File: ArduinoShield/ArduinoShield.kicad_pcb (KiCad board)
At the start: 2 copper layers, 47 x 45.7 mm, 45 parts, among them J1 Molex 1053131103, J2 Molex 1053131102, J3 Molex 1053131103, J4 Molex 1053131102, J5 Molex 1053131102, U1 MCP9808_DFN, U2 ALS31300, U3 BME280

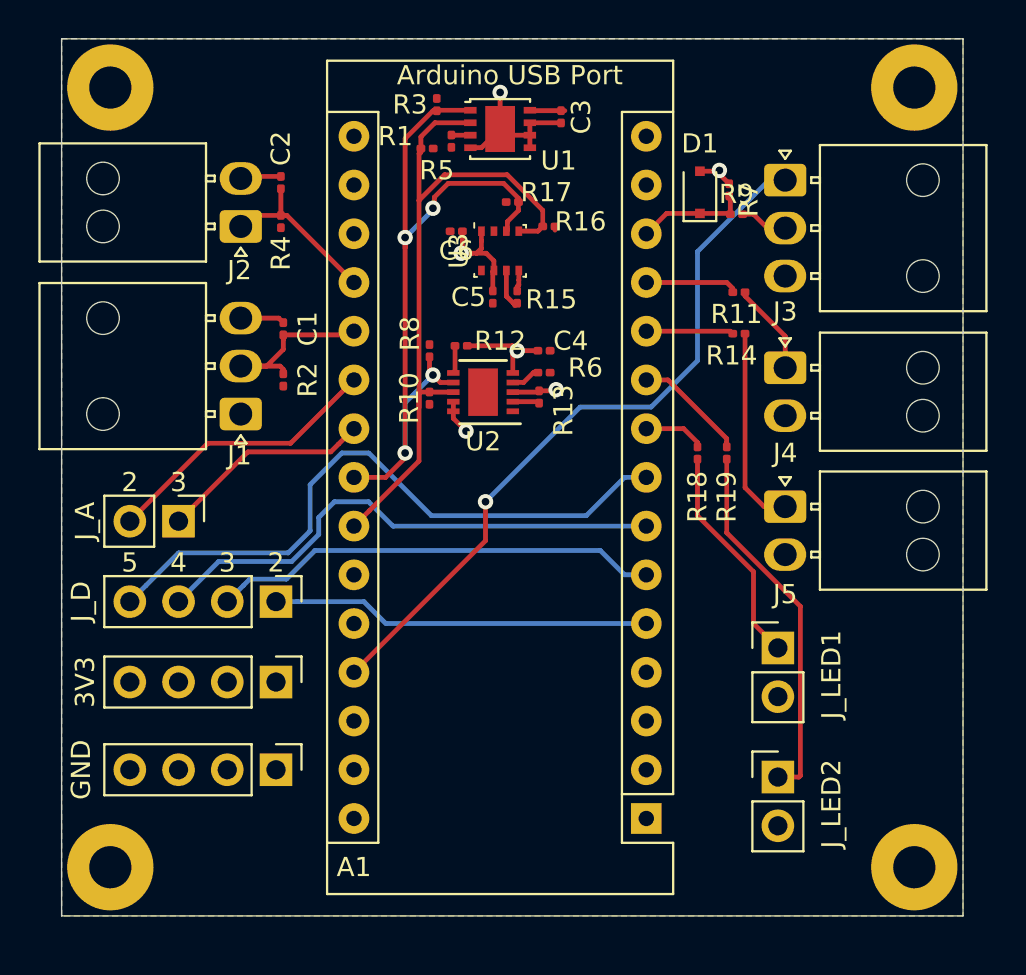
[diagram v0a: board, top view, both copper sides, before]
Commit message: Updated Hole size for Arduino, Created Footprint for bigger hole sizes
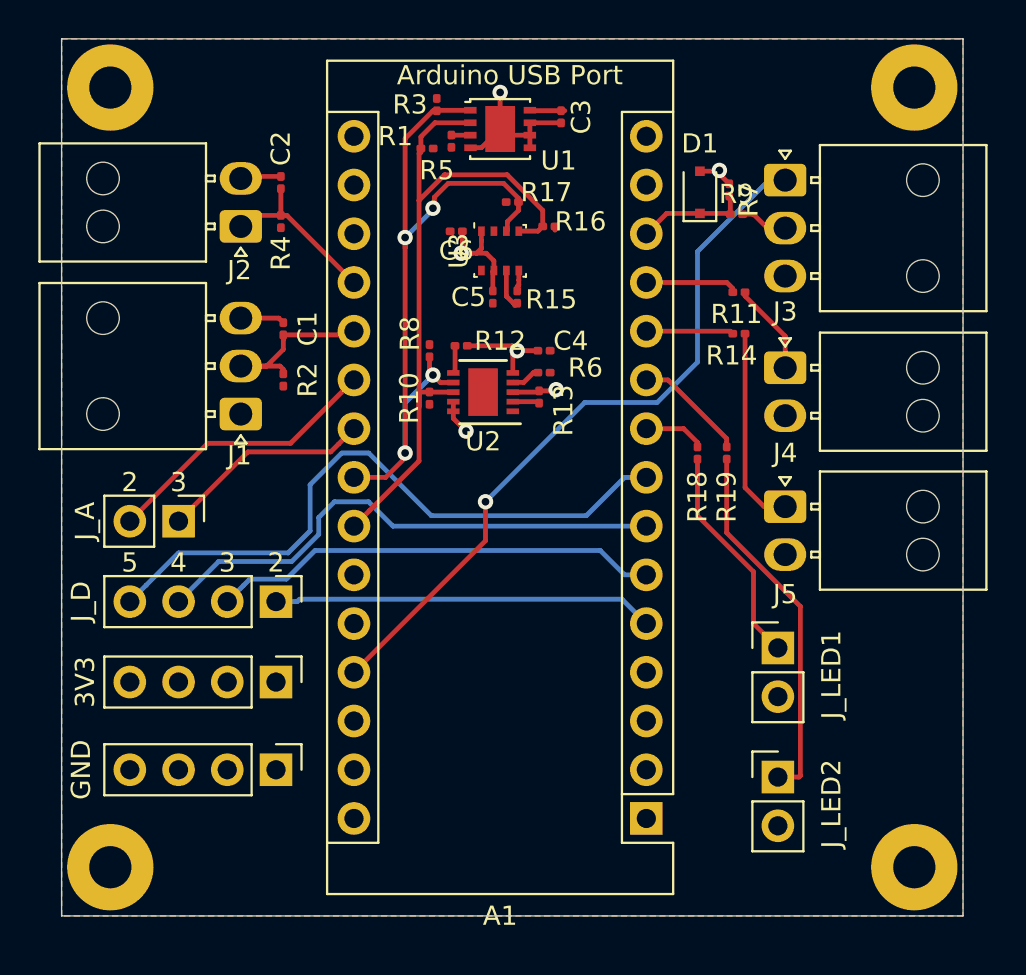
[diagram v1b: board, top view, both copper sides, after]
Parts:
- A1: footprint Module:Arduino_Nano -> ArduinoShield:Arduino_Nano

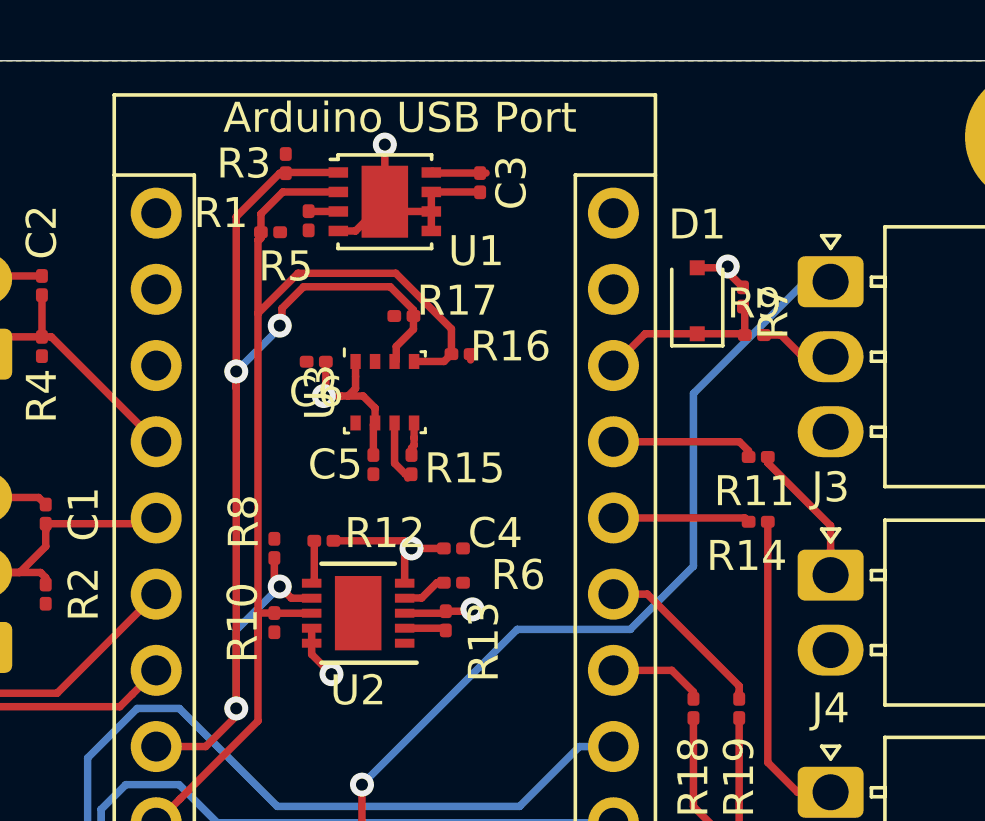
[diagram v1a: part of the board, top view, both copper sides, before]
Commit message: Modified part that was wrong in KiCad Library (MCP9808)
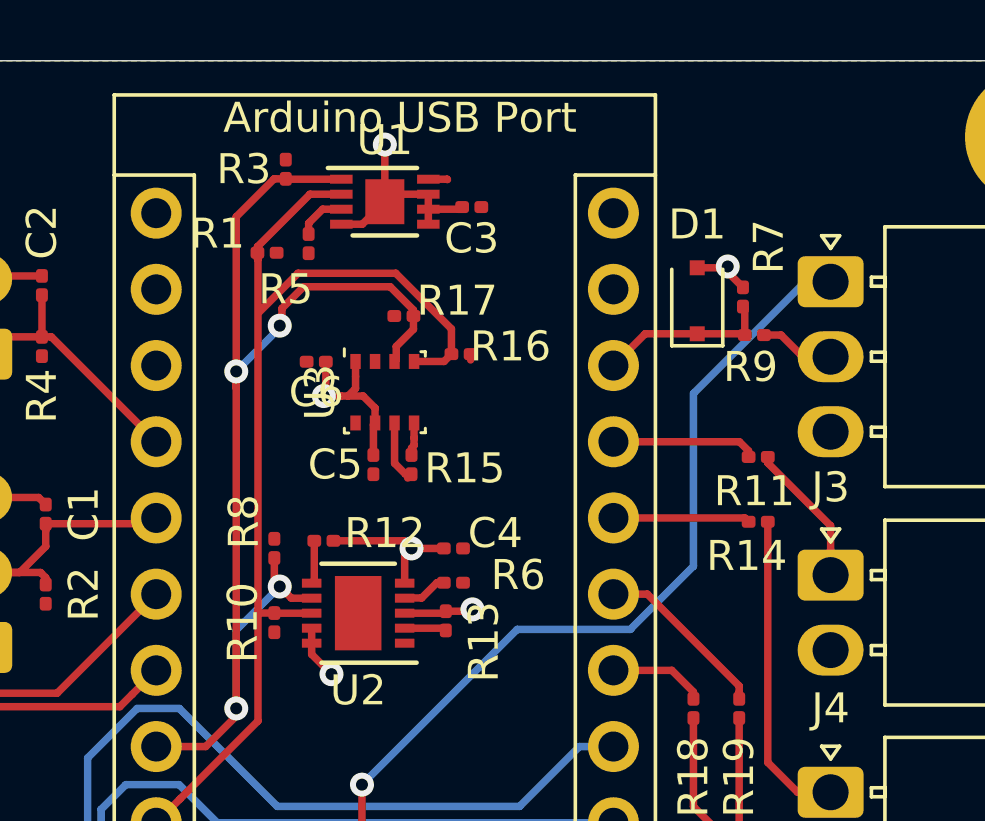
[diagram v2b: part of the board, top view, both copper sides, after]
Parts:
- U1: footprint Package_DFN_QFN:DFN-8-1EP_3x3mm_P0.65mm_EP1.55x2.4mm -> Package_DFN_QFN:DFN-8-1EP_3x2mm_P0.5mm_EP1.3x1.5mm
- moved C3 0.86 mm to (132.4, 70.9), turned to 180 degrees
- moved R5 0.76 mm to (127.0, 72.1)
- moved R1 0.70 mm to (125.6, 72.4)
- moved R3 0.19 mm to (126.2, 69.7)
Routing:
- net SCL: track 37.3 -> 35.9 mm
- net +3V3: track 4.53 -> 3.20 mm
- net Net-(R5-Pad2): track 0.99 -> 1.73 mm
- net GND: track 30.3 -> 29.7 mm
